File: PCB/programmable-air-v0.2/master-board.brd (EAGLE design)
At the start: 97.8 x 47 mm, 31 parts, among them J1 POWER_JACKTOE

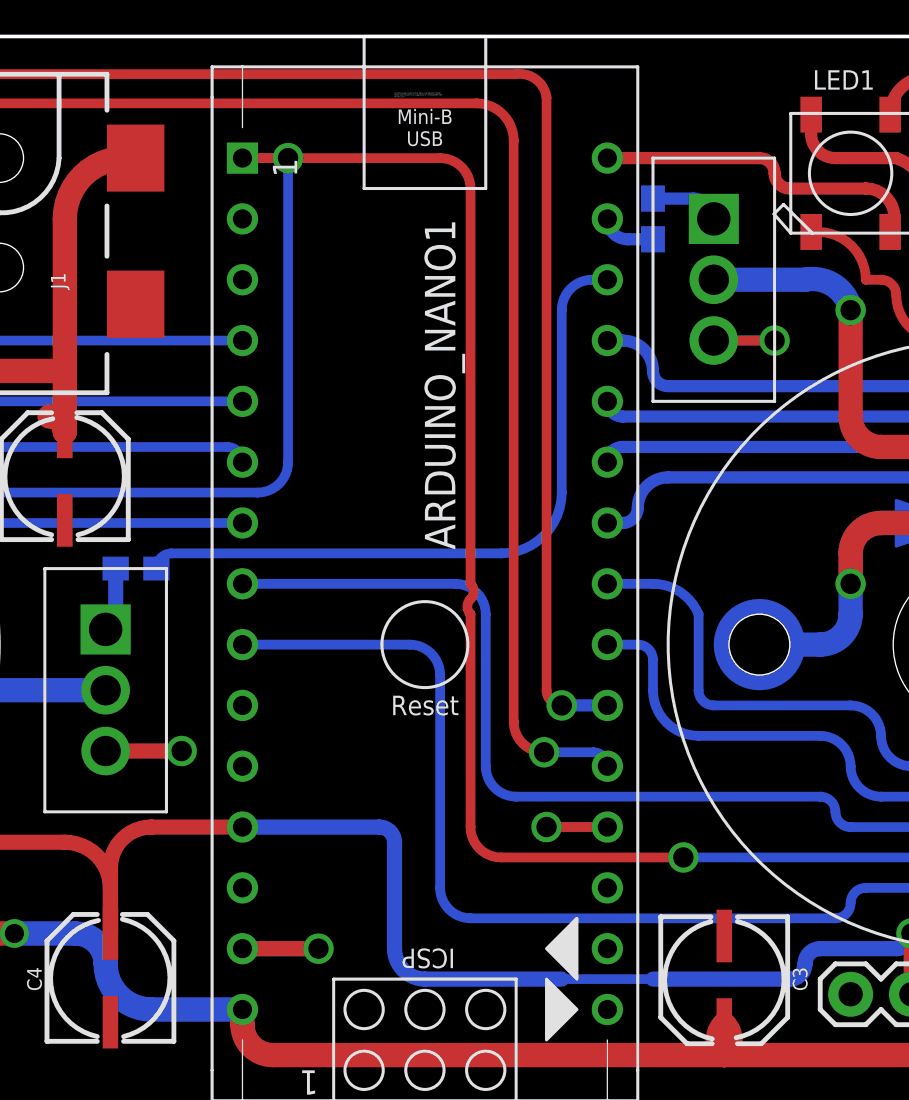
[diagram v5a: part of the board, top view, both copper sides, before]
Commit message: Minor fixes to slave PCB after assembly. Started work on test code for PCB v0.2
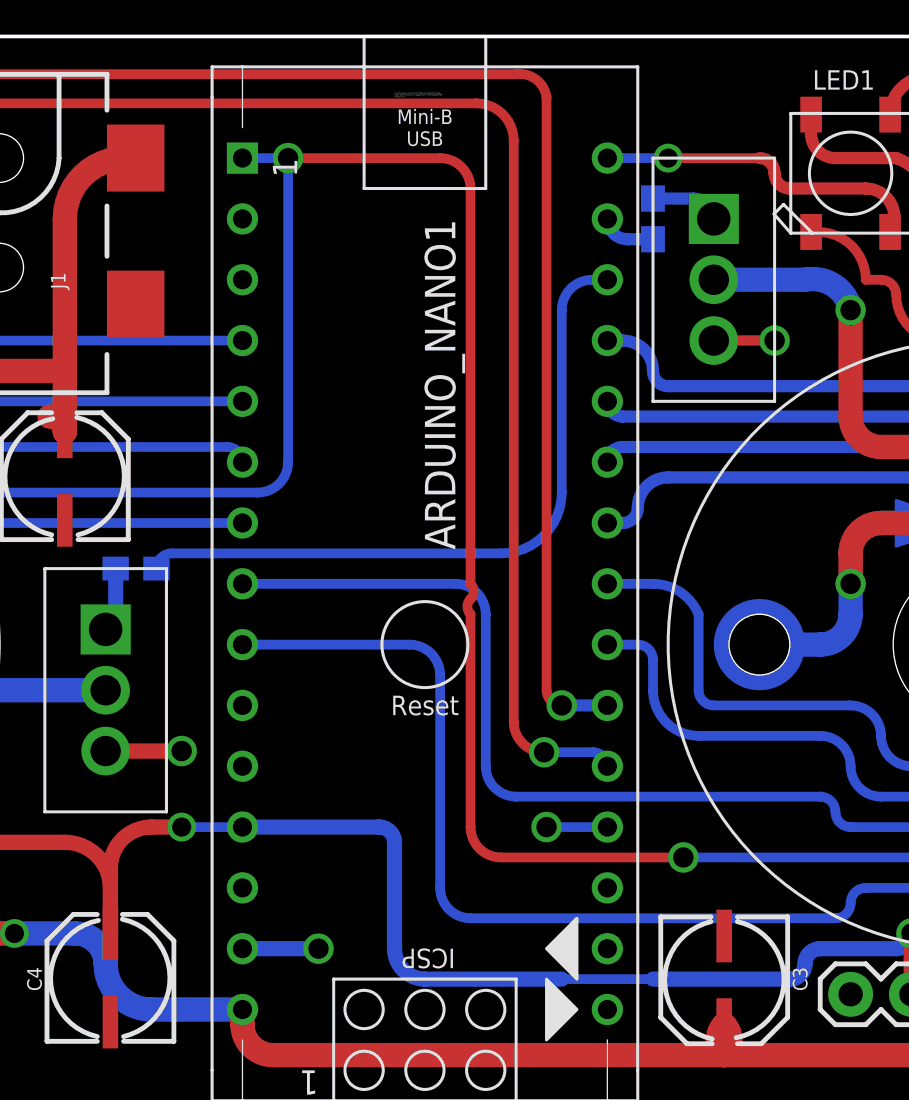
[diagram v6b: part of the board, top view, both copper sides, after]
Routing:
- net GND: track 59.3 -> 53.6 mm
- net N$13: track 147.1 -> 145.2 mm
- net VCC: vias 3 -> 4
- net N$8: vias 0 -> 1
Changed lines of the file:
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@@
 <contactref element="S4" pad="4"/>
 <wire x1="77.09" y1="38.825" x2="77.09" y2="38.99" width="0.508" layer="1"/>
-<wire x1="60.96" y1="13.97" x2="58.42" y2="13.97" width="0.4064" layer="1"/>
 <via x="58.42" y="13.97" extent="1-16" drill="0.85"/>
-<wire x1="60.96" y1="13.97" x2="58.42" y2="13.97" width="0.4064" layer="16"/>
 <polygon width="1.016" layer="16">
 <vertex x="0" y="44.45"/>
@@
 <vertex x="2.54" y="46.99" curve="90"/>
 </polygon>
-<wire x1="45.72" y1="8.89" x2="48.895" y2="8.89" width="0.635" layer="1"/>
 <via x="48.895" y="8.89" extent="1-16" drill="0.85"/>
 <wire x1="48.895" y1="8.89" x2="45.72" y2="8.89" width="0.635" layer="16"/>
@@
 <via x="67.945" y="34.29" extent="1-16" drill="0.85"/>
 <wire x1="67.945" y1="34.29" x2="65.405" y2="34.29" width="0.4064" layer="16"/>
+<wire x1="60.96" y1="13.97" x2="58.42" y2="13.97" width="0.4064" layer="16"/>
 <wire x1="13.5" y1="41.13" x2="13.5" y2="45.23" width="0" layer="19" extent="1-1"/>
 <wire x1="22.39" y1="45.23" x2="22.39" y2="41.13" width="0" layer="19" extent="1-1"/>
@@
 <contactref element="J2" pad="5"/>
 <contactref element="J3" pad="5"/>
-<wire x1="45.72" y1="41.91" x2="47.625" y2="41.91" width="0.4064" layer="1"/>
 <wire x1="47.625" y1="41.91" x2="53.975" y2="41.91" width="0.4064" layer="1"/>
 <wire x1="53.975" y1="41.91" x2="55.245" y2="40.64" width="0.4064" layer="1" curve="-90"/>
@@
 <via x="78.74" y="12.065" extent="1-16" drill="0.85"/>
 <wire x1="78.74" y1="12.065" x2="78.74" y2="6.985" width="0.4064" layer="16"/>
-<wire x1="45.72" y1="41.91" x2="47.625" y2="41.91" width="0.4064" layer="16"/>
 <via x="47.625" y="41.91" extent="1-16" drill="0.85"/>
 <wire x1="56.515" y1="12.7" x2="64.135" y2="12.7" width="0.4064" layer="1"/>
@@
 <wire x1="26.035" y1="27.305" x2="25.7175" y2="27.6225" width="0.4064" layer="16" curve="-90"/>
 <wire x1="26.035" y1="27.305" x2="31.75" y2="27.305" width="0.4064" layer="16"/>
+<wire x1="45.72" y1="41.91" x2="47.625" y2="41.91" width="0.4064" layer="16"/>
 </signal>
 <signal name="N$22">
@@
 <wire x1="67.31" y1="41.91" x2="67.945" y2="41.275" width="0.508" layer="1" curve="-90"/>
 <wire x1="67.945" y1="41.275" x2="68.58" y2="40.64" width="0.508" layer="1" curve="90"/>
-<wire x1="60.96" y1="41.91" x2="67.31" y2="41.91" width="0.508" layer="1"/>
 <wire x1="68.58" y1="40.64" x2="71.755" y2="40.64" width="0.508" layer="1"/>
+<wire x1="60.96" y1="41.91" x2="63.5" y2="41.91" width="0.4064" layer="16"/>
+<via x="63.5" y="41.91" extent="1-16" drill="0.8"/>
+<wire x1="63.5" y1="41.91" x2="67.31" y2="41.91" width="0.4064" layer="1"/>
 </signal>
 <signal name="N$12">
@@
 <wire x1="40.205" y1="9.52" x2="40.205" y2="12.265" width="0.635" layer="1"/>
 <wire x1="40.205" y1="12.265" x2="41.91" y2="13.97" width="0.635" layer="1" curve="-90"/>
-<wire x1="41.91" y1="13.97" x2="45.72" y2="13.97" width="0.635" layer="1"/>
+<wire x1="41.91" y1="13.97" x2="43.18" y2="13.97" width="0.635" layer="1"/>
 <wire x1="40.205" y1="9.52" x2="40.205" y2="11.425" width="0.635" layer="1"/>
 <wire x1="40.205" y1="11.425" x2="38.295" y2="13.335" width="0.635" layer="1" curve="90"/>
+<wire x1="45.72" y1="13.97" x2="43.18" y2="13.97" width="0.4064" layer="16"/>
+<via x="43.18" y="13.97" extent="1-16" drill="0.8"/>
 </signal>
 <signal name="N$20">
